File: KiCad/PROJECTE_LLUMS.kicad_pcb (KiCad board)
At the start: 2 copper layers, 100 x 65.2 mm, 62 parts, among them J1 CONNECTOR_MOTOR, J2 DE9_Pins_MountingHoles, J4 Conn_01x02_Pin, J5 DE9_Pins_MountingHoles, Q2 IRLZ44N, Q3 IRLZ44N, Q4 IRLZ44N, Q5 IRLZ44N, Q6 IRLZ44N, Q7 IRLZ44N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

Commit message: presentar
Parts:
- added K1: Fujitsu_FTR-LYAA005x, Relay_SMD:Relay_DPDT_Omron_G6S-2F, F.Cu at (145.0, 31.1)
- U7: value ~ -> PIC24HJ128GP502
- moved REF** 18.7 mm to (90.6, 55.0)
- moved J1 18.3 mm to (139.0, 62.1)
- moved REF** 17.8 mm to (185.8, 55.4)
- moved C3 17.6 mm to (101.5, 80.6)
- moved C4 17.6 mm to (95.5, 67.1)
- moved D8 17.6 mm to (93.0, 70.8)
- moved J4 17.6 mm to (101.2, 59.6)
- moved L1 17.6 mm to (92.3, 76.8)
- moved U5 17.6 mm to (106.9, 71.0)
- moved U4 14.5 mm to (131.8, 92.3)
- moved C1 14.5 mm to (119.8, 80.2)
- moved C10 14.5 mm to (99.6, 96.7)
- moved C11 14.5 mm to (96.7, 96.6)
- moved C2 14.5 mm to (119.8, 85.0)
- moved C5 14.5 mm to (122.8, 71.8)
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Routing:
- net +5V: track 139.4 -> 153.9 mm
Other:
- board size 100 x 65.2 mm -> 103.4 x 69.4 mm
- board text added: "12V"
- board text added: "GND"

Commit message: correccions Manel
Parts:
- added J3: Conn_01x05, Connector_PinHeader_2.54mm:PinHeader_1x05_P2.54mm_Vertical, F.Cu at (170.4, 10.7)
- K1: footprint Relay_SMD:Relay_DPDT_Omron_G6S-2F -> Relay_THT:Relay_1-Form-C_Schrack-RYII_RM3.2mm
- moved CARRETERA 71.8 mm to (195.2, 41.8), turned to -90 degrees
- moved ENCREUAMENT 62.5 mm to (184.8, 41.8), turned to -90 degrees
- moved DIURNA 54.8 mm to (174.3, 41.9), turned to -90 degrees
- moved MOTOR 51.0 mm to (142.1, 42.1), turned to -90 degrees
- moved INT_ESQ 50.0 mm to (163.6, 41.9), turned to -90 degrees
- moved INT_DRT 48.5 mm to (152.9, 42.0), turned to -90 degrees
- moved REF** 39.4 mm to (221.2, 38.1)
- moved K1 37.3 mm to (127.4, 64.0), turned to 90 degrees
- moved REF** 35.7 mm to (221.1, 117.2)
- moved REF** 16.9 mm to (90.0, 38.1)
- moved C3 5.65 mm to (101.3, 74.9)
- moved C4 5.65 mm to (95.3, 61.4)
- moved D8 5.65 mm to (92.8, 65.2)
- moved L1 5.65 mm to (92.1, 71.2)
- moved U5 5.65 mm to (106.7, 65.4)
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- renumbered SW1 to CARRETERA, SW3 to DIURNA, SW2 to ENCREUAMENT, SW5 to INT_DRT, SW6 to INT_ESQ, SW4 to MOTOR
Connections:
- net /microcontrolador//MCLR renamed VPP_MCLR
- U7 pad 4: unconnected-(U7-RB0-Pad4) -> DATA
- U7 pad 5: unconnected-(U7-RB1-Pad5) -> CLK
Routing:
- net +5V: track 153.9 -> 161.4 mm
- net INTERM. ESQ: track 57.4 -> 50.3 mm
- net ENCREUAMENT: track 68.2 -> 61.0 mm
- net INTERM. DRT: track 54.8 -> 47.7 mm
- net CARRETERA: track 73.8 -> 66.8 mm
- net NETEJA-FARS: track 59.6 -> 52.6 mm
- net DIURNA: track 62.3 -> 55.3 mm
- net +12V: track 69.4 -> 70.2 mm
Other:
- board size 103.4 x 69.4 mm -> 138.1 x 86.1 mm
- board text added: "S'HA DE POSAR EL GNDPWR"

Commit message: algo de routing
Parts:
- added TP_SCL1: TestPoint, Connector_PinHeader_2.54mm:PinHeader_1x01_P2.54mm_Vertical, F.Cu at (130.7, 99.1)
- added TP_SDA1: TestPoint, Connector_PinHeader_2.54mm:PinHeader_1x01_P2.54mm_Vertical, F.Cu at (127.1, 99.1)
- moved J3 117.5 mm to (96.3, 101.9), turned to 90 degrees
- moved C10 9.47 mm to (97.8, 87.4)
- moved U6 9.47 mm to (104.2, 87.7)
- moved C11 9.47 mm to (95.0, 87.3)
- moved J4 5.80 mm to (101.0, 48.2)
- moved C3 5.80 mm to (101.3, 69.1)
- moved C4 5.80 mm to (95.3, 55.6)
- moved D8 5.80 mm to (92.8, 59.4)
- moved L1 5.80 mm to (92.1, 65.4)
- moved U5 5.80 mm to (106.7, 59.6)
- moved REF** 0.10 mm to (90.0, 38.2)
- renumbered CARRETERA to SW1, ENCREUAMENT to SW2, DIURNA to SW3, MOTOR to SW4, INT_DRT to SW5, INT_ESQ to SW6
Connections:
- J3 pad 2: 5V -> +5V
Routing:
- net CARRETERA: track 66.8 -> 136.3 mm, vias 4 -> 6
- net +5V: track 161.4 -> 217.4 mm, vias 4 -> 6
- net ENCREUAMENT: track 61.0 -> 115.4 mm, vias 2 -> 4
- net DIURNA: track 55.3 -> 99.0 mm, vias 2 -> 4
- net VPP_MCLR: track 5.30 -> 48.2 mm, vias 0 -> 2
- net DATA: track 0.00 -> 40.0 mm, vias 0 -> 4
- net NETEJA-FARS: track 52.6 -> 92.2 mm
- net INTERM. ESQ: track 50.3 -> 89.5 mm, vias 0 -> 2
- net INTERM. DRT: track 47.7 -> 86.7 mm, vias 0 -> 2
- net CLK: track 0.00 -> 35.1 mm, vias 0 -> 2
- net +12V: track 70.2 -> 91.0 mm
- net I2C_SDA: track 35.8 -> 41.7 mm
- net I2C_SCL: track 31.4 -> 36.5 mm
- net +3V3: track 4.82 -> 4.30 mm
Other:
- board text added: "5V"
- board text added: "CLK"
- board text added: "DATA"
- board text added: "MCLR"
- board text added: "S'HAN DE POSAR MES TEST POINTS"

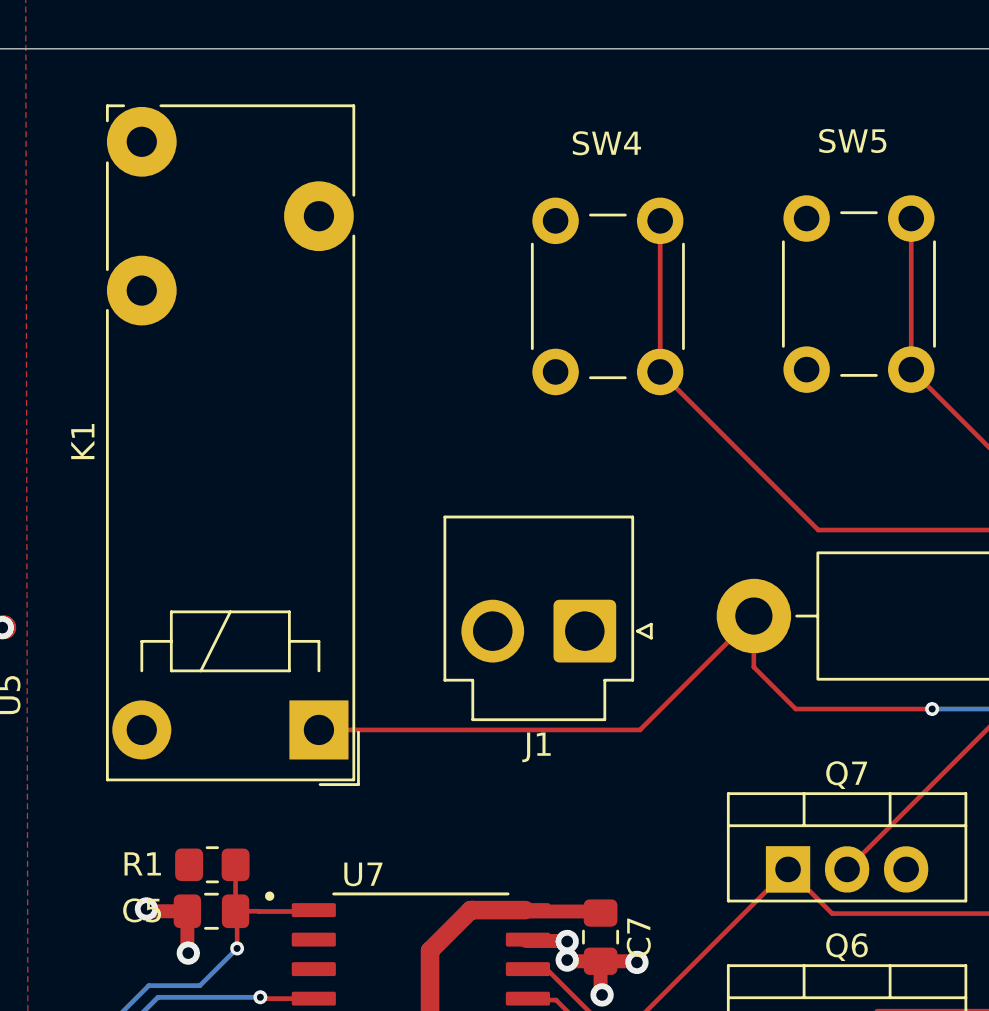
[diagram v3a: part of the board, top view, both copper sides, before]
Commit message: Connectors amb huellas
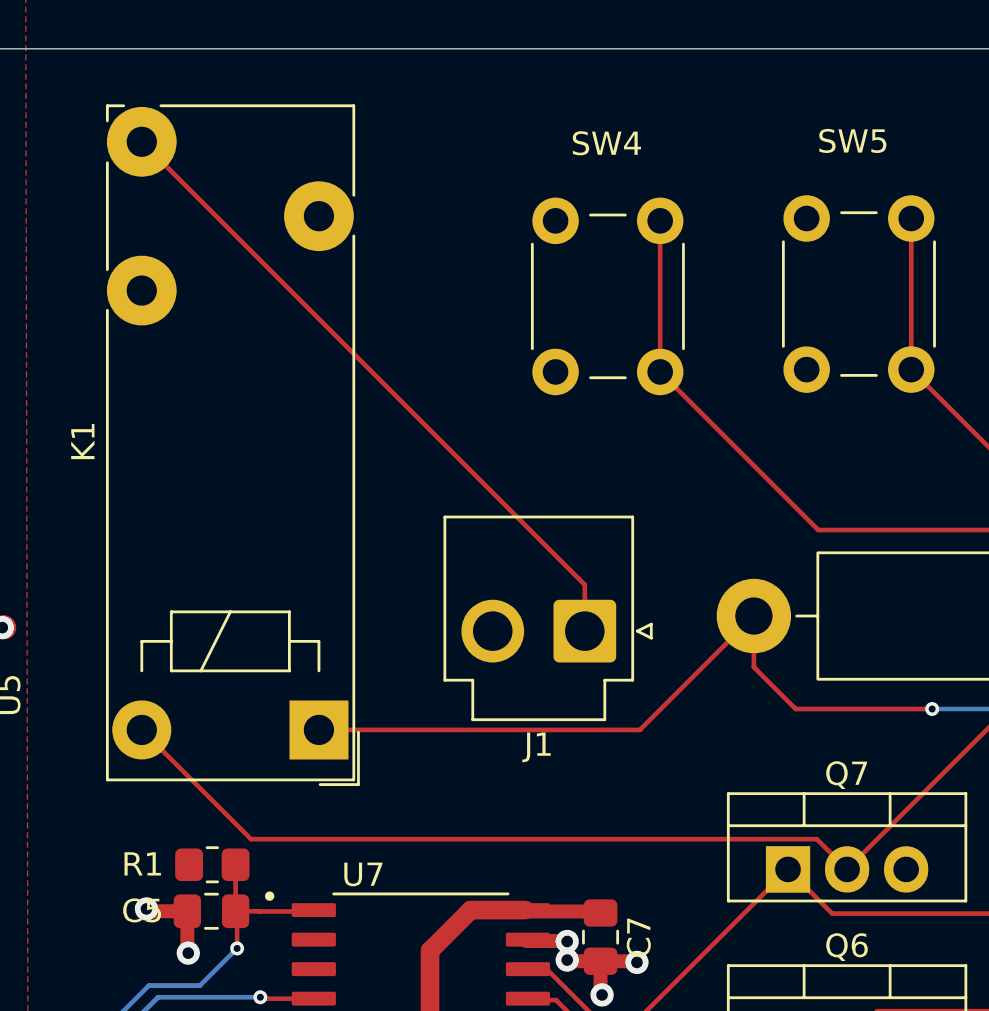
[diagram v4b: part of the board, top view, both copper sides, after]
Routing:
- net /llums/RELÉ: track 15.7 -> 48.6 mm
- net /llums/MOTOR: track 0.00 -> 28.9 mm
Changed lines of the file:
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@@
+	)
+	(segment
+		(start 138.8575 57.7575)
+		(end 138.8575 59.75)
+		(width 0.2)
+		(layer "F.Cu")
+		(net 38)
+	)
+	(segment
+		(start 119.8 38.7)
+		(end 138.8575 57.7575)
+		(width 0.2)
+		(layer "F.Cu")
+		(net 38)
+	)
+	(segment
+		(start 119.8 64)
+		(end 124.499 68.699)
+		(width 0.2)
+		(layer "F.Cu")
+		(net 39)
+	)
+	(segment
+		(start 124.499 68.699)
+		(end 148.839 68.699)
+		(width 0.2)
+		(layer "F.Cu")
+		(net 39)
 	)
 	(segment
@@
 		(width 0.2)
 		(layer "F.Cu")
+		(net 39)
+	)
+	(segment
+		(start 148.839 68.699)
+		(end 150.14 70)
+		(width 0.2)
+		(layer "F.Cu")

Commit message: coses
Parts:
- removed D2, D3, D4, D5, D6: LED, LED_THT:LED_D5.0mm
- removed R2, R3, R4, R5, R6: 1k, Relay_SMD:Relay_2P2T_10x6mm_TE_IMxxG
- added J10: Conn_01x02_Pin, TerminalBlock:TerminalBlock_MaiXu_MX126-5.0-02P_1x02_P5.00mm, F.Cu at (189.0, 65.4)
- added J6: Conn_01x02_Pin, TerminalBlock_Phoenix:TerminalBlock_Phoenix_MKDS-1,5-2-5.08_1x02_P5.08mm_Horizontal, F.Cu at (188.9, 98.7)
- added J7: Conn_01x02_Pin, TerminalBlock:TerminalBlock_MaiXu_MX126-5.0-02P_1x02_P5.00mm, F.Cu at (188.9, 110.8)
- added J8: Conn_01x02_Pin, TerminalBlock:TerminalBlock_MaiXu_MX126-5.0-02P_1x02_P5.00mm, F.Cu at (189.2, 86.3)
- added J9: Conn_01x02_Pin, TerminalBlock:TerminalBlock_MaiXu_MX126-5.0-02P_1x02_P5.00mm, F.Cu at (188.9, 76.3)
- added R50: 0, Resistor_SMD:R_0805_2012Metric_Pad1.20x1.40mm_HandSolder, F.Cu at (114.9, 70.9)
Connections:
- C3 pad 2: GND -> GNDPWR
- C4 pad 2: GND -> GNDPWR
- D8 pad 2: GND -> GNDPWR
- J4 pad 2: GND -> GNDPWR
- Q2 pad 2: /llums/C_LED3 -> /llums/A_LED3
- Q3 pad 2: /llums/C_LED2 -> /llums/A_LED2
- Q4 pad 2: /llums/C_LED5 -> /llums/A_LED5
- Q5 pad 2: /llums/C_LED4 -> /llums/A_LED4
- Q6 pad 2: /llums/C_LED6 -> /llums/A_LED6
- U5 pad 3: GND -> GNDPWR
- U5 pad 5: GND -> GNDPWR
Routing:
- net GND: track 113.1 -> 56.9 mm, vias 58 -> 43
- net GNDPWR: track 0.00 -> 56.3 mm, vias 0 -> 15
- net /llums/A_LED5: track 3.53 -> 43.9 mm, vias 1 -> 0
- net /llums/A_LED4: track 5.42 -> 45.7 mm, vias 1 -> 0
- net /llums/A_LED2: track 3.87 -> 42.4 mm
- net /llums/A_LED6: track 5.76 -> 43.8 mm, vias 1 -> 0
- net /llums/A_LED3: track 4.95 -> 42.3 mm, vias 1 -> 0
- net +12V: track 91.0 -> 120.8 mm, vias 1 -> 0
- net /llums/C_LED6: track 13.7 -> 0.00 mm
- net /llums/C_LED5: track 13.3 -> 0.00 mm
- net /llums/C_LED4: track 12.9 -> 0.00 mm
- net /llums/C_LED2: track 12.3 -> 0.00 mm
- net /llums/C_LED3: track 11.8 -> 0.00 mm
- net NETEJA-FARS: track 92.2 -> 90.0 mm
- net +5V: vias 6 -> 8
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- added copper zone on B.Cu, net GNDPWR

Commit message: presentació
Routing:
- net +5V: vias 8 -> 6
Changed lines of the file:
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@@
 	)
 	(segment
-		(start 151.26 112.76)
-		(end 142.7 112.76)
+		(start 130.74 112.76)
+		(end 151.26 112.76)
 		(width 0.6)
 		(layer "F.Cu")
@@
 	)
 	(segment
-		(start 130.74 112.76)
-		(end 129 114.5)
-		(width 0.6)
-		(layer "F.Cu")
-		(net 3)
-	)
-	(segment
 		(start 95.3 65.875)
 		(end 98.55 69.125)
@@
 	(segment
 		(start 129 114.5)
-		(end 117.7 114.5)
+		(end 130.74 112.76)
+		(width 0.6)
+		(layer "F.Cu")
+		(net 3)
+	)
+	(segment
+		(start 117.7 114.5)
+		(end 129 114.5)
 		(width 0.6)
 		(layer "F.Cu")
@@
 	)
 	(segment
-		(start 136.5 112.76)
-		(end 130.74 112.76)
-		(width 0.6)
-		(layer "F.Cu")
-		(net 3)
-	)
-	(segment
 		(start 101.1 90)
 		(end 101.201 90.101)
@@
 	)
 	(segment
-		(start 117.7 114.5)
-		(end 116.605 113.405)
-		(width 0.6)
-		(layer "F.Cu")
-		(net 3)
-	)
-	(segment
 		(start 108.36 112.96)
 		(end 116.605 112.96)
@@
 	)
 	(segment
-		(start 116.605 113.405)
-		(end 116.605 112.96)
+		(start 116.605 112.96)
+		(end 116.605 113.405)
 		(width 0.6)
 		(layer "F.Cu")
@@
 		(end 95.3 65.875)
 		(width 1)
+		(layer "F.Cu")
+		(net 3)
+	)
+	(segment
+		(start 116.605 113.405)
+		(end 117.7 114.5)
+		(width 0.6)
 		(layer "F.Cu")
 		(net 3)
@@
 	)
 	(via
-		(at 142.7 112.76)
-		(size 0.8)
-		(drill 0.4)
-		(layers "F.Cu" "B.Cu")
-		(net 3)
-	)
-	(via
 		(at 117.2 90.05)
 		(size 0.6)
@@
 	)
 	(via
-		(at 136.5 112.76)
-		(size 0.8)
-		(drill 0.4)
-		(layers "F.Cu" "B.Cu")
-		(net 3)
-	)
-	(via
 		(at 100.7 91.8)
 		(size 0.8)
@@
 		(width 0.6)
 		(layer "B.Cu")
-		(net 3)
-	)
-	(segment
-		(start 136.5 112.76)
-		(end 142.7 112.76)
-		(width 0.6)
-		(layer "B.Cu")

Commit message: correccions manel
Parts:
- R10, R11, R12, R7, R8, R9: moved to B.Cu
- moved REF** 21.9 mm to (199.2, 117.0)
- moved REF** 21.9 mm to (199.3, 37.9)
- moved Q4 7.04 mm to (154.4, 82.8)
- moved Q5 7.04 mm to (154.4, 90.2)
- moved Q6 7.04 mm to (154.4, 75.5)
- moved Q7 7.04 mm to (154.4, 68.0)
- moved Q3 7.04 mm to (154.4, 97.7)
- moved Q2 7.04 mm to (154.3, 104.8)
- moved R7 6.11 mm to (165.5, 104.0)
- moved R10 5.91 mm to (165.9, 67.2)
- moved R8 5.48 mm to (165.6, 96.8)
- moved R9 5.32 mm to (165.6, 89.4)
- moved R11 5.31 mm to (165.9, 74.4)
- moved R12 5.19 mm to (165.8, 82.1)
- moved J10 4.88 mm to (187.1, 60.9), turned to 90 degrees
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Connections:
- C6 pad 1: +5V -> +3V3
- C7 pad 1: +5V -> +3V3
- U7 pad 13: +5V -> +3V3
- U7 pad 28: +5V -> +3V3
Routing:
- net CARRETERA: track 136.3 -> 10.7 mm, vias 6 -> 0
- net +12V: track 120.8 -> 0.00 mm
- net ENCREUAMENT: track 115.4 -> 10.1 mm, vias 4 -> 0
- net DIURNA: track 99.1 -> 9.63 mm, vias 4 -> 0
- net NETEJA-FARS: track 90.0 -> 10.1 mm
- net INTERM. ESQ: track 89.5 -> 10.0 mm, vias 2 -> 0
- net INTERM. DRT: track 86.7 -> 10.7 mm, vias 2 -> 0
- net +5V: track 217.4 -> 164.6 mm, vias 6 -> 2
- net +3V3: track 4.30 -> 31.9 mm, vias 2 -> 20
- net /llums/A_LED4: track 45.7 -> 32.4 mm
- net /llums/A_LED2: track 42.4 -> 31.3 mm, vias 1 -> 0
- net /llums/A_LED5: track 43.9 -> 33.9 mm
- net /llums/A_LED3: track 42.3 -> 33.7 mm
- net GNDPWR: track 56.3 -> 50.2 mm, vias 15 -> 18
- net /llums/A_LED6: track 43.8 -> 38.4 mm
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- added copper zone on F.Cu, net +12V
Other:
- board size 138.1 x 86.1 mm -> 116.3 x 86.1 mm

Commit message: routing def
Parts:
- moved SW5 10.9 mm to (141.2, 42.0)
- moved SW4 10.8 mm to (152.0, 42.0)
- turned R10 to 90 degrees
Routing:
- net CARRETERA: track 10.7 -> 125.3 mm, vias 0 -> 2
- net ENCREUAMENT: track 10.1 -> 104.2 mm
- net DIURNA: track 9.63 -> 87.8 mm
- net INTERM. ESQ: track 10.0 -> 78.9 mm
- net INTERM. DRT: track 10.7 -> 71.0 mm
- net NETEJA-FARS: track 10.1 -> 65.3 mm
- net /llums/RELÉ: track 49.2 -> 52.8 mm
- net +3V3: track 31.9 -> 28.7 mm
- net UART_RX: track 39.0 -> 39.2 mm, vias 2 -> 1
- net UART_TX: track 29.6 -> 29.5 mm, vias 4 -> 1
- net I2C_SDA: vias 2 -> 0
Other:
- board text added: "- I2C - CAN - UART LEDS ALIMENTACIO: - DC-DC - REGULADOR - MICRO"
- board text added: "S'HAN DE POSAR MES TEST POINTS:"
- board text removed: "S'HA DE POSAR EL GNDPWR"
- board text removed: "S'HAN DE POSAR MES TEST POINTS"
